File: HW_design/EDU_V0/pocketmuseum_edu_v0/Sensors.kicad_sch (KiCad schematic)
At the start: 17 parts, among them Q301 BSS138, Q302 BSS138, Q303 BSS138, U1 ICM-20948, U3 ICP20100

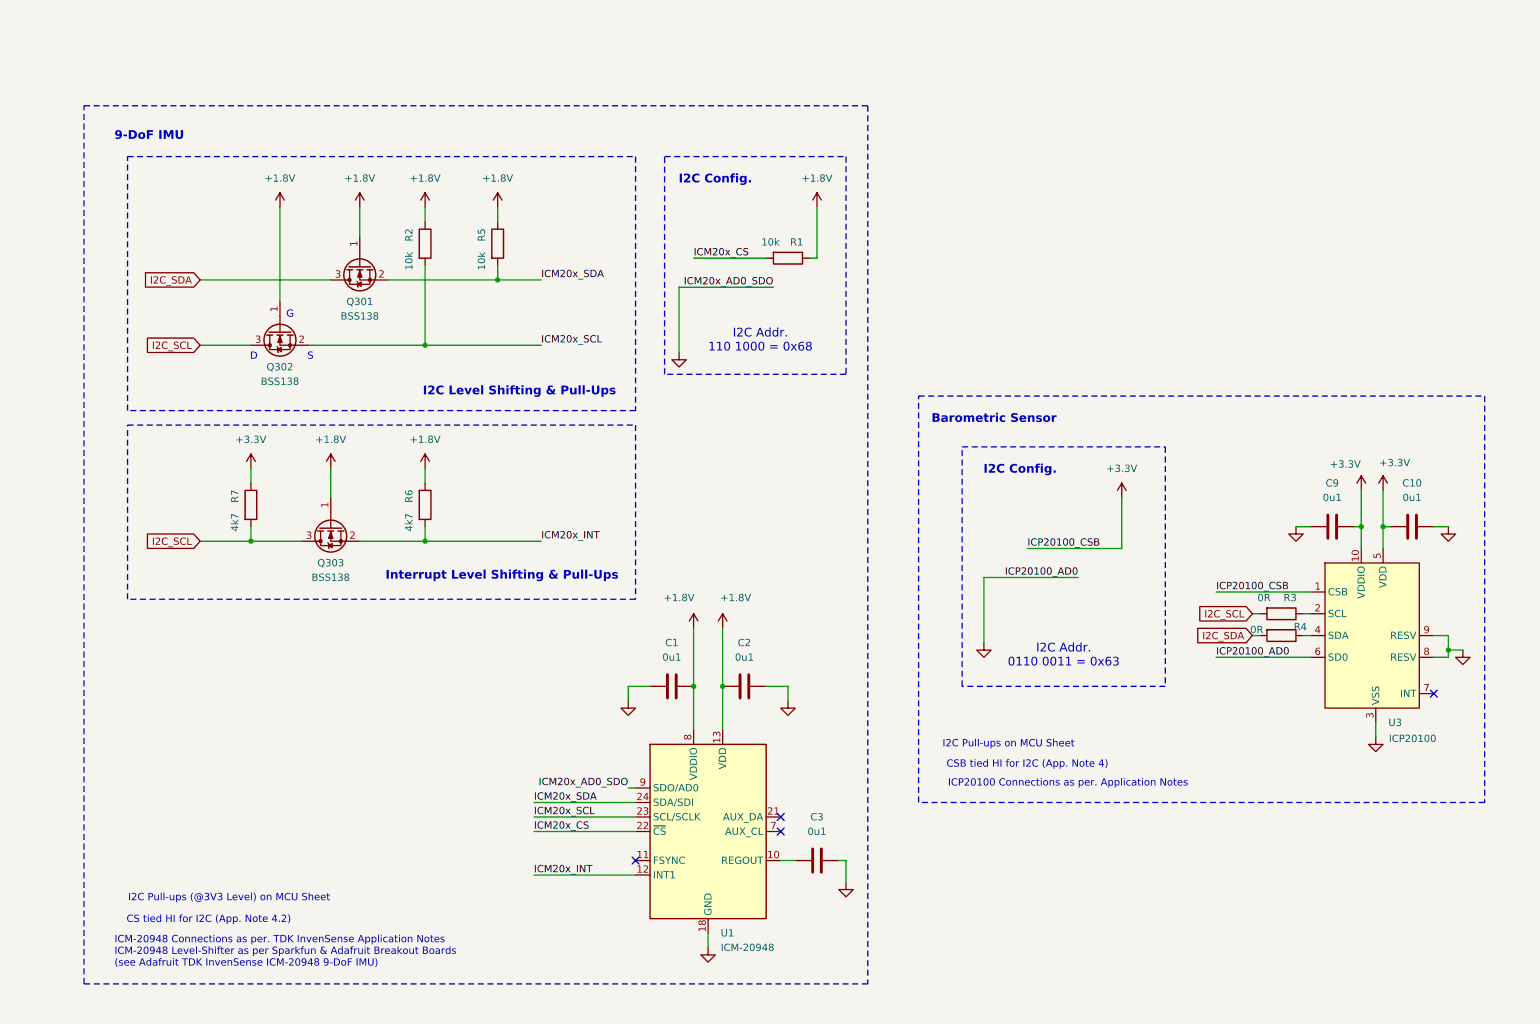
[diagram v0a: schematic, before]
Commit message: [EDUV0] Cleaned-up uSD card
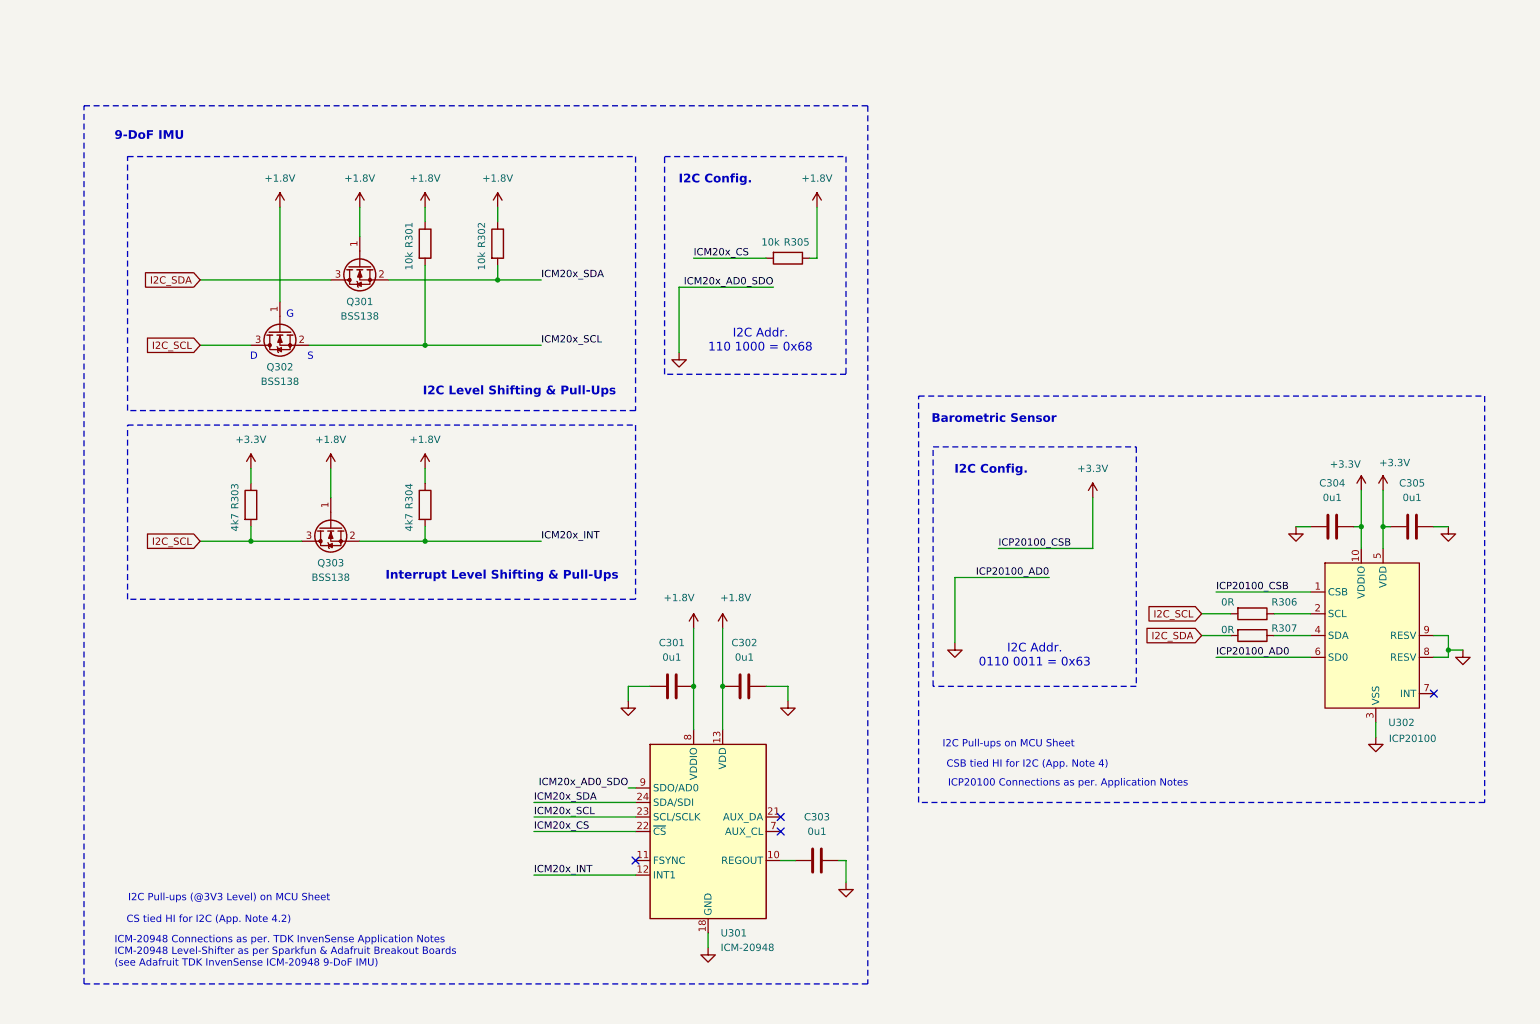
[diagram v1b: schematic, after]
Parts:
- renumbered C1 to C301, C2 to C302, C3 to C303, C9 to C304, C10 to C305, R2 to R301, R5 to R302, R7 to R303, R6 to R304, R1 to R305, R3 to R306, R4 to R307, U1 to U301, U3 to U302
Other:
- moved on the sheet: R306, R307

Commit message: Updated Readme
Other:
- company: (none) -> Bucharest Applied STEAM Museum
- title: (none) -> POCKETMUSEUM EDU V0
- moved on the sheet: C301, C302, C303, C304, C305, Q301, Q302, Q303, R301, R302, R303, R304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

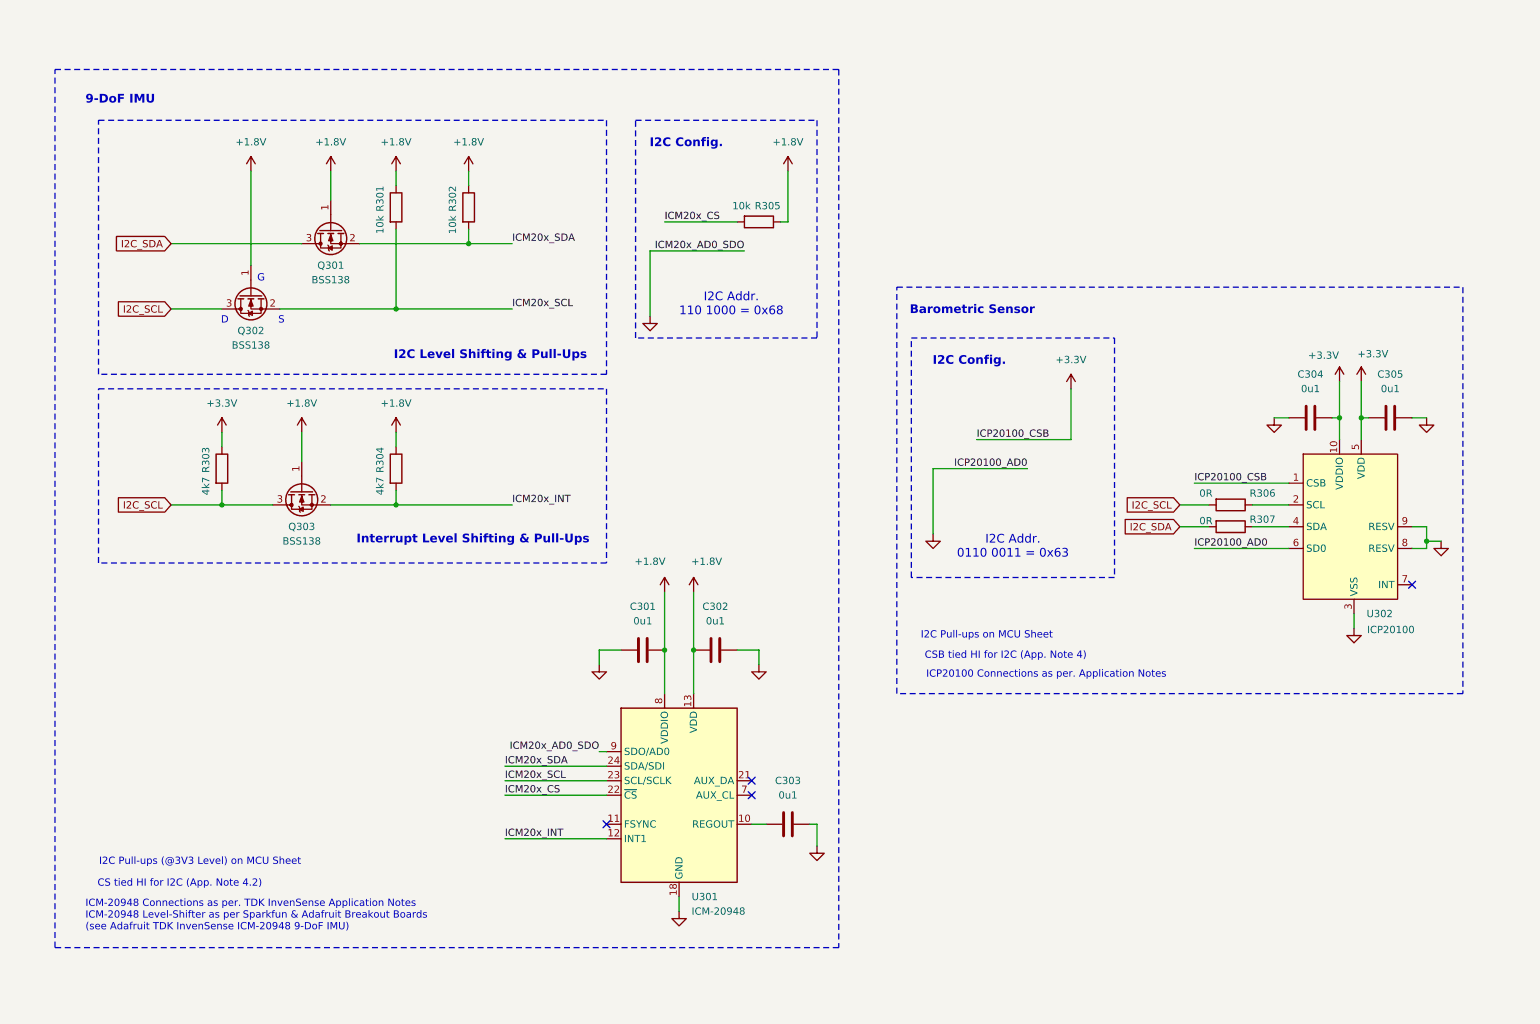
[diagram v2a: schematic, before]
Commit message: Added Mic & Light Sensor to EDU_V0
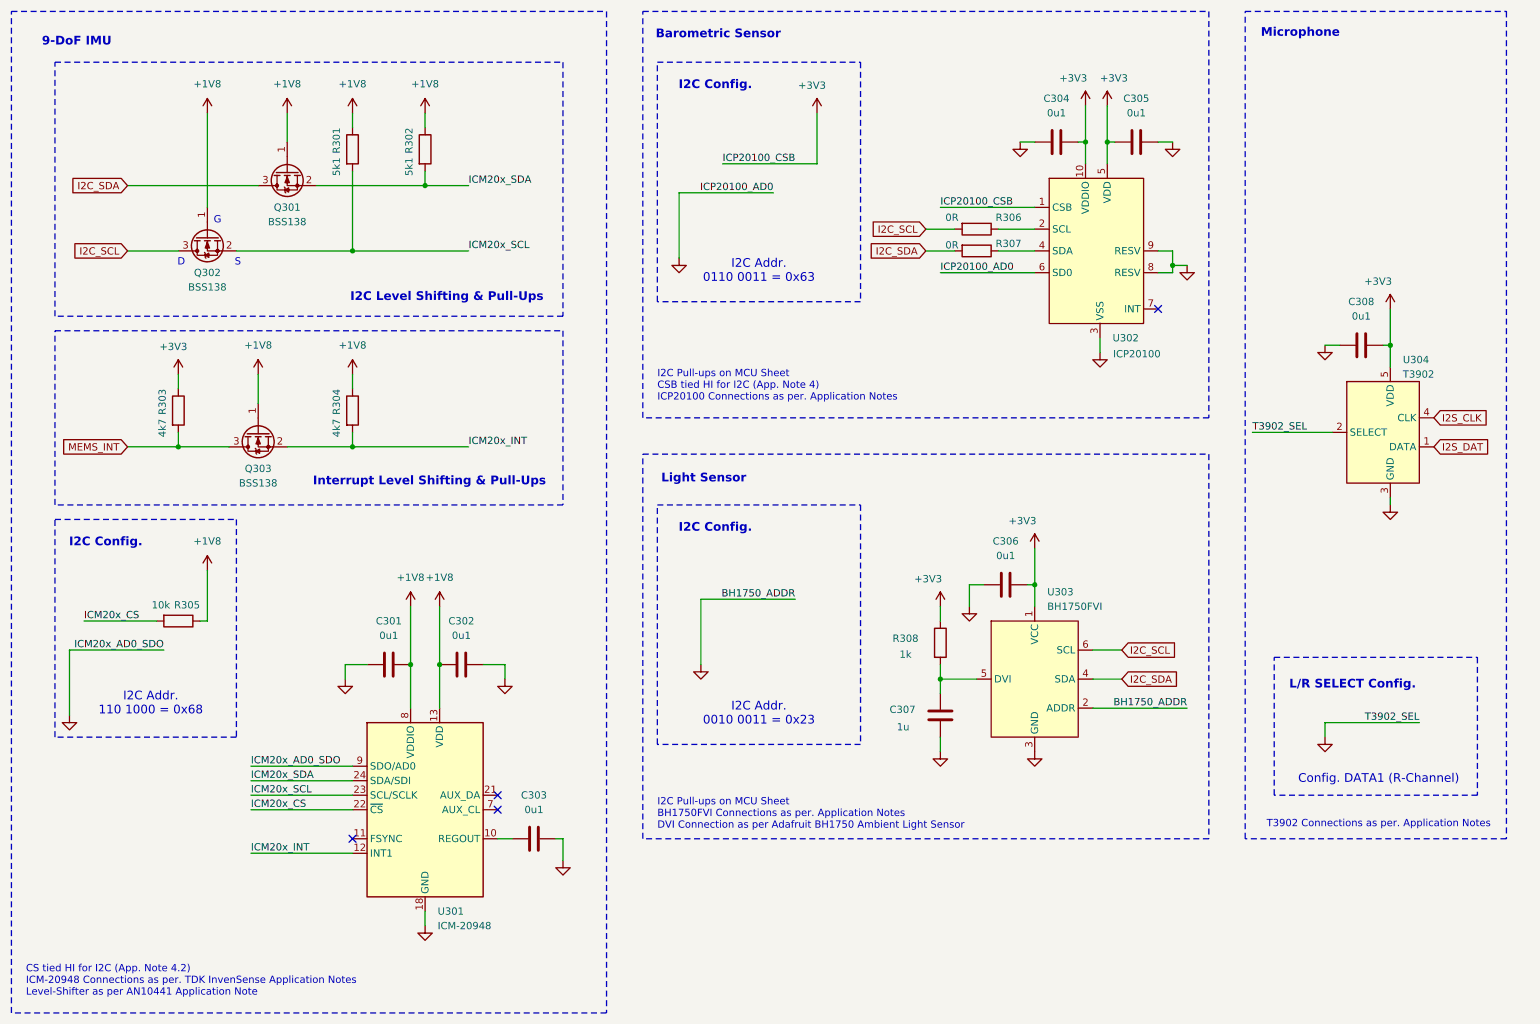
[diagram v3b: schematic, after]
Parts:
- added C306, C308: 0u1, Capacitor_SMD:C_0402_1005Metric, symbol Device:C
- added C307: 1u, Capacitor_SMD:C_0402_1005Metric, symbol Device:C
- added R308: 1k, Resistor_SMD:R_0402_1005Metric, symbol Device:R
- added U303: BH1750FVI, WSOF:XDCR_BH1750FVI-TR, symbol BH1750:BH1750FVI
- added U304: T3902, MMICT:MMIC, symbol BH1750:T3902
- R301, R302: value 10k -> 5k1; footprint Resistor_SMD:R_0603_1608Metric -> Resistor_SMD:R_0402_1005Metric
- R303, R304: footprint Resistor_SMD:R_0603_1608Metric -> Resistor_SMD:R_0402_1005Metric
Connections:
- net GND: now also C306.2, C307.2, C308.2, U303.2 (ADDR), U303.3 (GND), U304.2 (SELECT), U304.3 (GND)
- net I2C_SCL: now also U303.6 (SCL); no longer Q303.3 (D), R303.2
- net I2C_SDA: now also U303.4 (SDA)
- net +1.8V renamed +1V8
- net +3.3V renamed +3V3
- net +3V3: now also C306.1, C308.1, R308.1, U303.1 (VCC), U304.5 (VDD)
- new net: C307.1, R308.2, U303.5 (DVI)
- new net I2S_CLK: U304.4 (CLK)
- new net I2S_DAT: U304.1 (DATA)
- new net MEMS_INT: Q303.3 (D), R303.2
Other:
- note added: "CS tied HI for I2C (App. Note 4.2) ICM-20948 Connections as per. TDK InvenSense Application Notes Level-Shifter as per AN10441 Application Note"
- note added: "Config. DATA1 (R-Channel)"
- note added: "I2C Addr. 0010 0011 = 0x23"
- note added: "I2C Pull-ups on MCU Sheet BH1750FVI Connections as per. Application Notes DVI Connection as per Adafruit BH1750 Ambient Light Sensor"
- note added: "I2C Pull-ups on MCU Sheet CSB tied HI for I2C (App. Note 4) ICP20100 Connections as per. Application Notes"
- note added: "L/R SELECT Config."
- note added: "Light Sensor"
- note added: "Microphone"
- note added: "T3902 Connections as per. Application Notes"
- note removed: "CS tied HI for I2C (App. Note 4.2)"
- note removed: "CSB tied HI for I2C (App. Note 4)"
- note removed: "I2C Pull-ups (@3V3 Level) on MCU Sheet"
- note removed: "I2C Pull-ups on MCU Sheet"
- note removed: "ICM-20948 Connections as per. TDK InvenSense Application Notes ICM-20948 Level-Shifter as per Sparkfun & Adafruit Breakout Boards (see Adafruit TDK InvenSense ICM-20948 9-DoF IMU)"
- note removed: "ICP20100 Connections as per. Application Notes"
- moved on the sheet: C301, C302, C303, C304, C305, Q301, Q302, Q303, R301, R302, R303, R304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

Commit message: Diagram review complete
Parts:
- C301: value 0u1 -> 1u
- R303, R304: value 4k7 -> 5k1
- R305: footprint Resistor_SMD:R_0603_1608Metric -> Resistor_SMD:R_0402_1005Metric
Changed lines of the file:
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@@
 	)
 	(junction
+		(at 88.9 132.08)
+		(diameter 0)
+		(color 0 0 0 0)
+	)
+	(junction
 		(at 219.71 62.23)
 		(diameter 0)
@@
 	(wire
 		(pts
+			(xy 88.9 132.08) (xy 91.44 132.08)
+		)
+		(stroke
+			(width 0)
+			(type default)
+		)
+	)
+	(wire
+		(pts
 			(xy 74.93 134.62) (xy 74.93 132.08)
 		)
@@
 	(wire
 		(pts
-			(xy 91.44 121.92) (xy 91.44 132.08)
+			(xy 88.9 121.92) (xy 88.9 132.08)
 		)
 		(stroke
@@
 	(wire
 		(pts
-			(xy 86.36 121.92) (xy 86.36 132.08)
+			(xy 88.9 132.08) (xy 86.36 132.08)
 		)
 		(stroke
@@
 			)
 		)
-		(property "Value" "4k7"
+		(property "Value" "5k1"
 			(at 73.406 90.678 90)
 			(effects
@@
 			)
 		)
-		(property "Footprint" "Resistor_SMD:R_0603_1608Metric"
+		(property "Footprint" "Resistor_SMD:R_0402_1005Metric"
 			(at 45.72 122.682 90)
 			(effects
@@
 	)
 	(symbol
-		(lib_id "power:+3.3V")
-		(at 86.36 121.92 0)
-		(unit 1)
-		(exclude_from_sim no)
-		(in_bom yes)
-		(on_board yes)
-		(dnp no)
-		(fields_autoplaced yes)
-		(property "Reference" "#PWR041"
-			(at 86.36 125.73 0)
-			(effects
-				(font
-					(size 1.27 1.27)
-				)
-				(hide yes)
-			)
-		)
-		(property "Value" "+1V8"
-			(at 86.36 116.84 0)
-			(effects
-				(font
-					(size 1.27 1.27)
-				)
-			)
-		)
-		(property "Footprint" ""
-			(at 86.36 121.92 0)
-			(effects
-				(font
-					(size 1.27 1.27)
-				)
-				(hide yes)
-			)
-		)
-		(property "Datasheet" ""
-			(at 86.36 121.92 0)
-			(effects
-				(font
-					(size 1.27 1.27)
-				)
-				(hide yes)
-			)
-		)
-		(property "Description" "Power symbol creates a global label with name \"+3.3V\""
-			(at 86.36 121.92 0)
-			(effects
-				(font
-					(size 1.27 1.27)
-				)
-				(hide yes)
-			)
-		)
-		(pin "1"
-		)
-		(instances
-			(project "pocketmuseum_edu_v0"
-				(path "/4bede6f6-420d-49b9-8d53-bd69095749c2/36cdbd28-8810-4657-96de-41aba4386ff5"
-					(reference "#PWR041")
-					(unit 1)
-				)
-			)
-		)
-	)
-	(symbol
 		(lib_id "power:+5V")
 		(at 208.28 34.29 0)
@@
 			)
 		)
-		(property "Value" "0u1"
+		(property "Value" "1u"
 			(at 82.55 127 90)
 			(effects
@@
 	(symbol
 		(lib_id "power:+3.3V")
-		(at 91.44 121.92 0)
+		(at 88.9 121.92 0)
 		(unit 1)
 		(exclude_from_sim no)
@@
 		(fields_autoplaced yes)
 		(property "Reference" "#PWR042"
-			(at 91.44 125.73 0)
+			(at 88.9 125.73 0)
 			(effects
 				(font
@@
 		)
 		(property "Value" "+1V8"
-			(at 91.44 116.84 0)
+			(at 88.9 116.84 0)
 			(effects
 				(font
@@
 		)
 		(property "Footprint" ""
-			(at 91.44 121.92 0)
+			(at 88.9 121.92 0)
 			(effects
 				(font
@@
 		)
 		(property "Datasheet" ""
-			(at 91.44 121.92 0)
+			(at 88.9 121.92 0)
 			(effects
 				(font
@@
 		)
 		(property "Description" "Power symbol creates a global label with name \"+3.3V\""
-			(at 91.44 121.92 0)
+			(at 88.9 121.92 0)
 			(effects
 				(font
@@
 			)
 		)
-		(property "Value" "4k7"
+		(property "Value" "5k1"
 			(at 42.926 90.678 90)
 			(effects
